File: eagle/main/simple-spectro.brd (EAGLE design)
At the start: 99.1 x 73.7 mm, 53 parts, among them CON1 BAT, CON2 SPI, CON3 SPI, CON4 VIBR, IC1 32U4, IC2 MCP73831T, IC3 MCP1703-33, IC4 DMP1045U or DMG2302, U1 TMP75DGK, X1 8MHz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

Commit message: working on vibration
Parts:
- added Q6: BSP75, infineon:PG-SOT-223
- moved CON4 33.8 mm to (24.1, 5.08), flipped to the bottom, turned to 270 degrees
- moved R20 31.6 mm to (7.62, 8.26), flipped to the bottom, turned to 180 degrees
- moved U$7 1.27 mm to (24.8, 12.1)
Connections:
- new net N$14: CON4.2, Q6.2
- new net N$8: Q6.1, R20.2
- net A5: now also R20.1
- net GND: now also Q6.3
- net VCC: now also CON4.1
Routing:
- net A5: track 0.00 -> 103.6 mm, vias 0 -> 2
- net GND: track 93.9 -> 116.9 mm
- net N$8: track 0.00 -> 10.3 mm
- net VCC: track 333.9 -> 338.3 mm
- net N$14: track 0.00 -> 3.89 mm
- net D12*: track 90.1 -> 88.8 mm

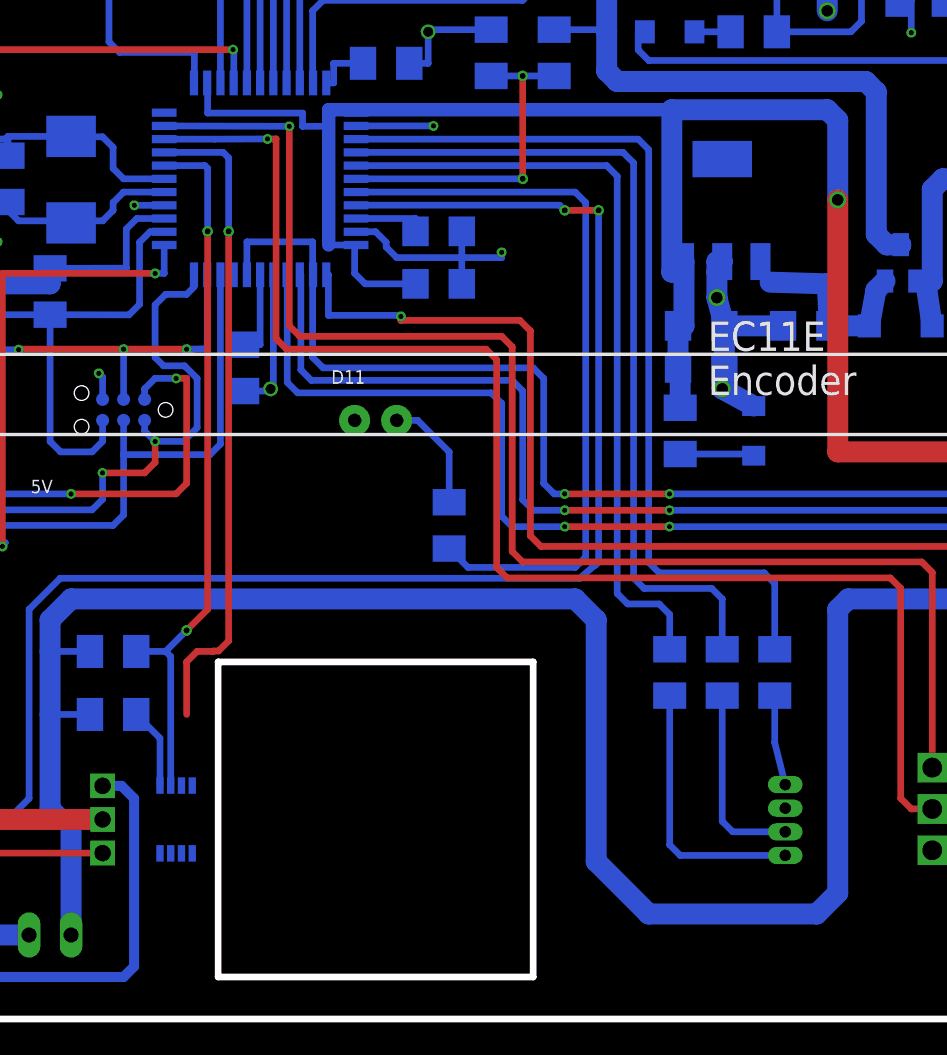
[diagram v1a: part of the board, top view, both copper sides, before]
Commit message: final design for price quote 1206 elecrow
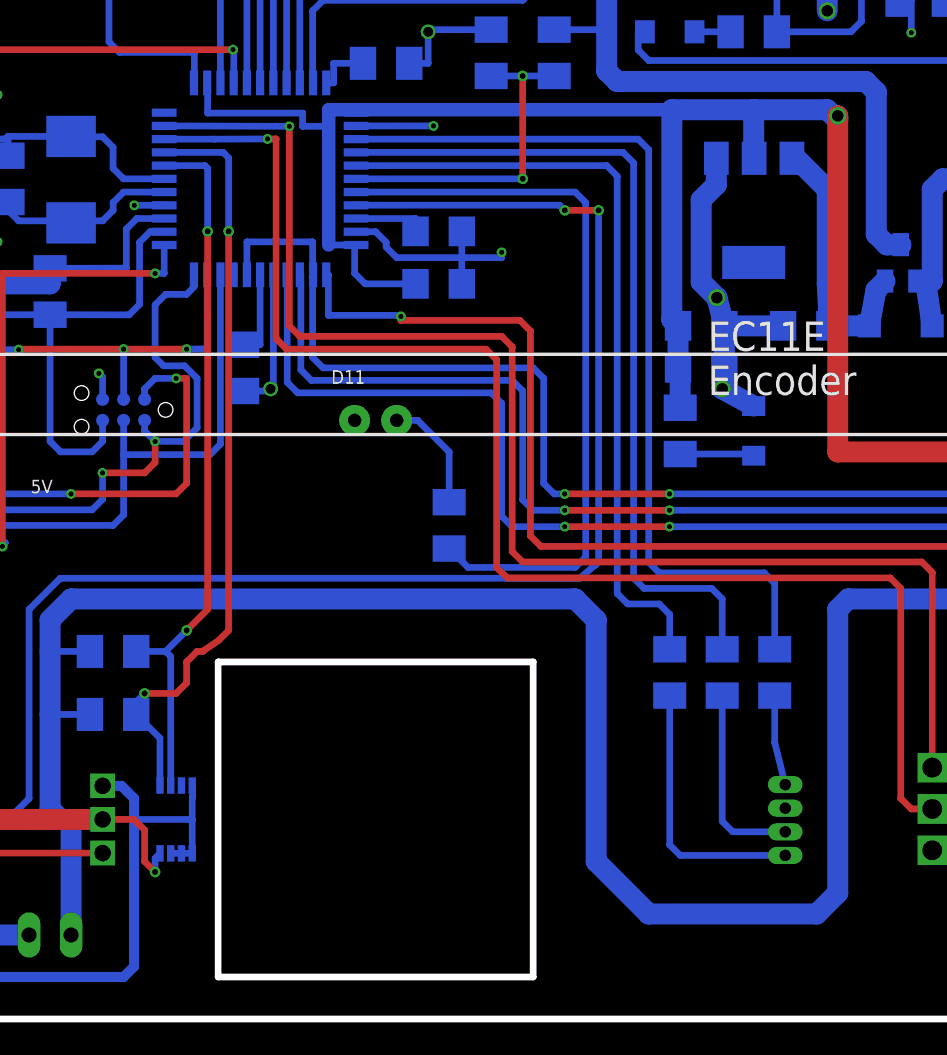
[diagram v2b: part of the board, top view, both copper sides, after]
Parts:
- removed IC3: MCP1703-33, linear:SOT223
- added IC5: LM1117S-3.3, burr-brown:SOT223
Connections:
- net GND: now also IC5.1; no longer IC3.2
- net VCC: now also IC5.2; no longer IC3.3
- net VDD: now also IC5.3; no longer IC3.1
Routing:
- net GND: track 116.9 -> 131.8 mm
- net VCC: track 338.3 -> 346.1 mm, vias 3 -> 4
- net VDD: track 13.4 -> 16.6 mm
- net SDA: track 44.4 -> 46.3 mm, vias 1 -> 2

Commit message: work on 0805
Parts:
- C1, C10, C2, C3, C6, C7, C8, C9: device resistor:C1206 -> rcl:C0805K
- C4, C5: device dp_devices:C1206 -> rcl:C0805K
- R1, R10, R11, R12, R13, R14, R15, R16, R17, R18, R19, R2, R20, R3, R4, R5, R6, R7, R8, R9: device rcl:M1206 -> rcl:R0805
- moved C4 10.9 mm to (77.5, 55.2), turned to 180 degrees
- moved C5 2.62 mm to (73.0, 69.2)
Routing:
- net GND: track 131.8 -> 138.0 mm, vias 16 -> 15
- net N$15: track 66.7 -> 69.2 mm
- net VBAT1: track 61.1 -> 63.3 mm
- net VCC: track 346.1 -> 347.9 mm
- net N$6: track 4.49 -> 3.88 mm

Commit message: pcb v1.4 elecrow
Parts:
- R16, R17, R18, R19, R3: value 10K -> 10k
- moved R11 0.17 mm to (24.1, 44.2)
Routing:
- net RESET: track 59.2 -> 58.1 mm

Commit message: move the pot to prevent contact with battery
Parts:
- moved POT 40.0 mm to (6.35, 22.9)
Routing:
- net N$2: track 19.0 -> 72.7 mm
- net D11*: track 89.2 -> 46.5 mm

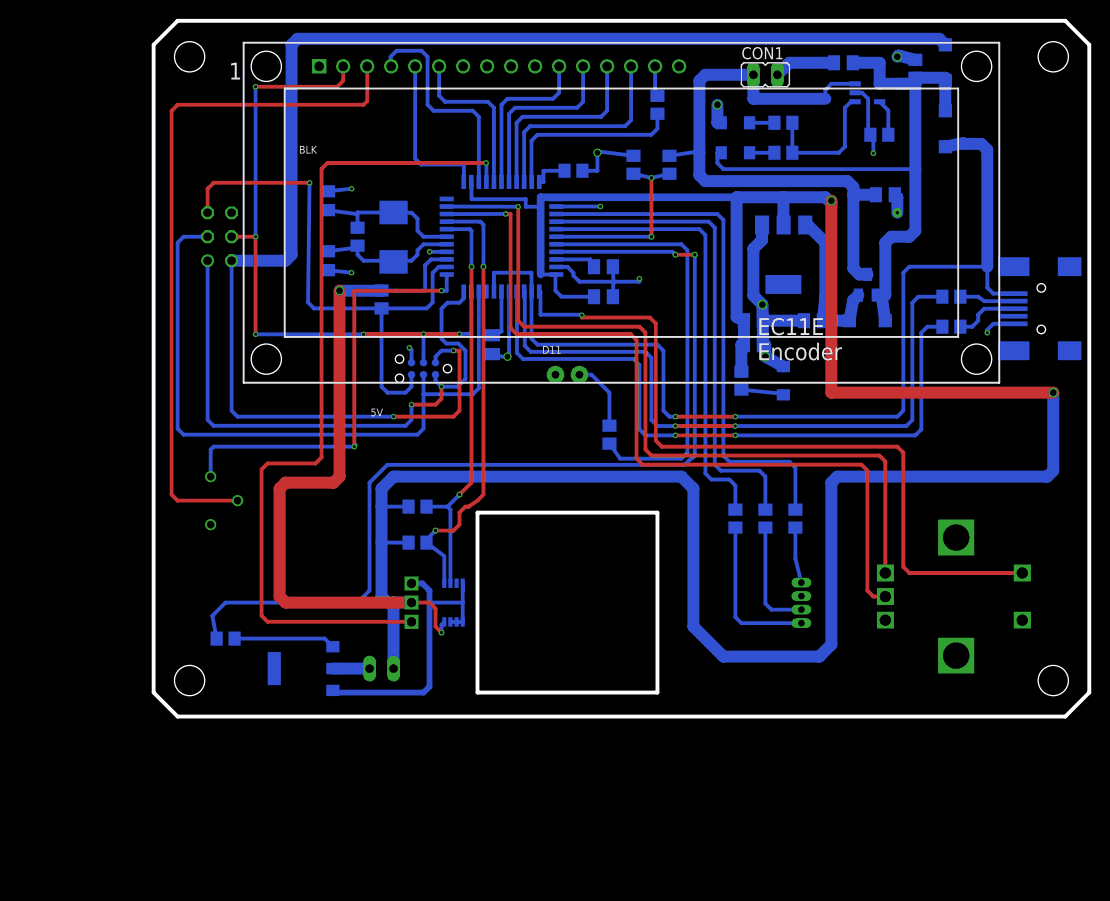
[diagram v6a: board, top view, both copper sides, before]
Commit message: update box to scratch the battery
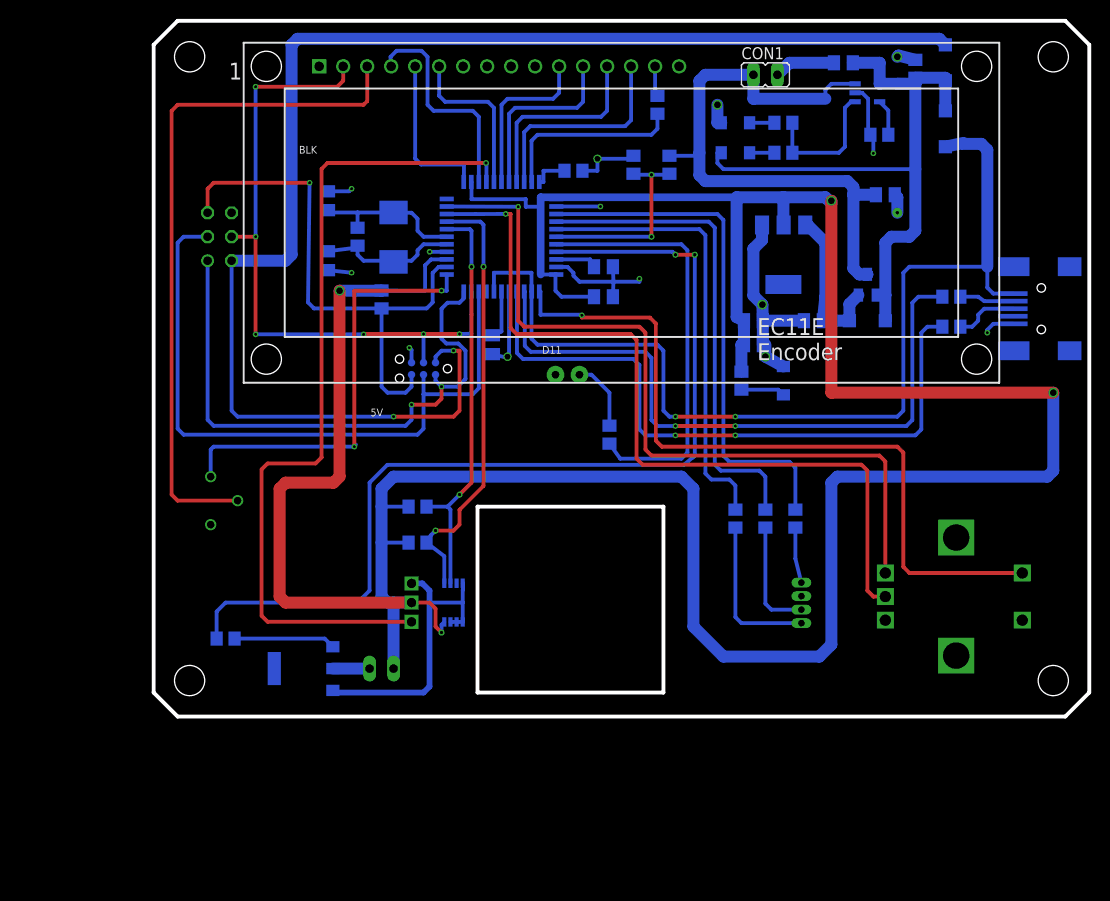
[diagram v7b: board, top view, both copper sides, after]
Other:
- outline, holes or cut-outs redrawn

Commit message: add temperature and battery sensor for model B
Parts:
- U1: value TMP75DGK -> NCT75DMR2G
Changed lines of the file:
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@@
 <element name="POT" library="dp_devices" package="TRIMMER_3362P" value="10k" x="6.35" y="22.86" rot="MR90"/>
 <element name="CON1" library="jumper" package="JP1" value="BAT" x="64.77" y="67.945" rot="R270"/>
-<element name="U1" library="ti_tmp" package="MSOP8" value="TMP75DGK" x="31.75" y="12.065" rot="MR180">
+<element name="U1" library="ti_tmp" package="MSOP8" value="NCT75DMR2G" x="31.75" y="12.065" rot="MR180">
 <attribute name="LCSC" value="C94387" x="24.13" y="4.445" size="1.778" layer="28" rot="MR180" display="off"/>
 </element>
